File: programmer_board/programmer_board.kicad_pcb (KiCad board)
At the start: 2 copper layers, 99.1 x 86.4 mm, 20 parts, among them J1 8bit_thing_bus_connector, J2 greenpak_i2c, U1 Pico, U2 74AHCT573, U3 74AHCT573, U4 74AHCT573, U5 74LVC245, U6 SLG46826G

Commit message: Pico programmer: remove some redundant traces and fix 3d model
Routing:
- net /D1_OUT: track 89.2 -> 87.5 mm
- net /D6_OUT: track 72.6 -> 71.8 mm
- net /D5_OUT: track 74.5 -> 73.7 mm
- net /D4_OUT: track 79.0 -> 78.2 mm
- net /D3_OUT: track 84.5 -> 83.7 mm
- net /D2_OUT: track 87.4 -> 86.6 mm
- net /D0_OUT: track 91.3 -> 90.5 mm
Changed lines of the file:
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@@
     (pad "20" smd roundrect (at 2.865 -2.925 90) (size 1.48 0.41) (layers "F.Cu" "F.Paste" "F.Mask") (roundrect_rratio 0.05)
       (net 5 "+5V") (pinfunction "VDD") (pintype "power_in"))
+    (model "${KICAD6_3DMODEL_DIR}/Package_SO.3dshapes/TSSOP-20_4.4x6.5mm_P0.65mm.wrl"
+      (offset (xyz 0 0 0))
+      (scale (xyz 1 1 1))
+      (rotate (xyz 0 0 0))
+    )
   )
   (footprint "imported_footprints:RPi_Pico_SMD_TH" (layer "F.Cu")
@@
   (segment (start 107.8445 56.0285) (end 107.569 55.753) (width 0.4) (layer "F.Cu") (net 6))
   (segment (start 85.3225 49.022) (end 85.3225 49.8055) (width 0.4) (layer "F.Cu") (net 6))
-  (segment (start 56.145 61.2035) (end 55.9015 60.96) (width 0.4) (layer "F.Cu") (net 6))
   (segment (start 56.145 63.1775) (end 56.145 64.247205) (width 0.4) (layer "F.Cu") (net 6))
   (segment (start 55.495 67.964797) (end 55.441509 67.911306) (width 0.4) (layer "F.Cu") (net 6))
@@
   (segment (start 78.218837 52.233503) (end 81.086 55.100666) (width 0.2) (layer "F.Cu") (net 43))
   (segment (start 81.086 56.761326) (end 81.855171 57.530497) (width 0.2) (layer "F.Cu") (net 43))
-  (segment (start 93.786 55.930996) (end 93.786 56.761326) (width 0.2) (layer "F.Cu") (net 43))
   (segment (start 81.855171 57.530497) (end 83.058503 57.530497) (width 0.2) (layer "F.Cu") (net 43))
   (segment (start 70.254126 57.546994) (end 73.551501 54.249619) (width 0.2) (layer "F.Cu") (net 43))
@@
   (segment (start 93.136 56.761326) (end 93.472 57.097326) (width 0.2) (layer "F.Cu") (net 44))
   (segment (start 73.951002 54.153558) (end 75.41856 52.686) (width 0.2) (layer "F.Cu") (net 44))
-  (segment (start 93.136 55.930996) (end 93.136 56.761326) (width 0.2) (layer "F.Cu") (net 44))
   (segment (start 75.41856 52.686) (end 78.045 52.686) (width 0.2) (layer "F.Cu") (net 44))
   (segment (start 73.951002 54.415098) (end 73.951002 54.153558) (width 0.2) (layer "F.Cu") (net 44))
@@
   (segment (start 90.600433 53.132493) (end 92.486 55.01806) (width 0.2) (layer "F.Cu") (net 45))
   (segment (start 83.529501 58.329499) (end 86.2965 55.5625) (width 0.2) (layer "F.Cu") (net 45))
-  (segment (start 92.486 55.930996) (end 92.486 56.761326) (width 0.2) (layer "F.Cu") (net 45))
   (segment (start 67.086 56.88394) (end 68.548056 58.345996) (width 0.2) (layer "F.Cu") (net 45))
   (segment (start 92.486 56.761326) (end 92.837 57.112326) (width 0.2) (layer "F.Cu") (net 45))
@@
   (segment (start 74.750004 54.746056) (end 74.750004 54.49429) (width 0.2) (layer "F.Cu") (net 46))
   (segment (start 88.454006 53.531994) (end 90.434954 53.531994) (width 0.2) (layer "F.Cu") (net 46))
-  (segment (start 91.839501 55.934497) (end 91.839501 56.764827) (width 0.2) (layer "F.Cu") (net 46))
   (segment (start 92.202 57.127326) (end 92.202 83.932) (width 0.2) (layer "F.Cu") (net 46))
   (segment (start 75.878278 53.930996) (end 77.511996 53.930996) (width 0.2) (layer "F.Cu") (net 47))
@@
   (segment (start 90.269475 53.931495) (end 91.186 54.84802) (width 0.2) (layer "F.Cu") (net 47))
   (segment (start 77.511996 53.930996) (end 78.486 54.905) (width 0.2) (layer "F.Cu") (net 47))
-  (segment (start 91.186 55.930996) (end 91.186 56.761326) (width 0.2) (layer "F.Cu") (net 47))
   (segment (start 88.624505 53.931495) (end 90.269475 53.931495) (width 0.2) (layer "F.Cu") (net 47))
   (segment (start 87.9865 55.88) (end 87.9865 55.13448) (width 0.2) (layer "F.Cu") (net 48))
@@
   (segment (start 89.76633 54.330996) (end 90.536 55.100666) (width 0.2) (layer "F.Cu") (net 48))
   (segment (start 77.836 56.761326) (end 80.619173 59.544499) (width 0.2) (layer "F.Cu") (net 48))
-  (segment (start 90.536 55.930996) (end 90.536 56.761326) (width 0.2) (layer "F.Cu") (net 48))
   (segment (start 87.9865 55.13448) (end 88.789985 54.330996) (width 0.2) (layer "F.Cu") (net 48))
   (segment (start 77.150702 54.330996) (end 77.836 55.016294) (width 0.2) (layer "F.Cu") (net 48))
@@
   (segment (start 77.836 55.016294) (end 77.836 55.930996) (width 0.2) (layer "F.Cu") (net 48))
   (segment (start 90.932 87.742) (end 106.68 103.49) (width 0.2) (layer "F.Cu") (net 48))
-  (segment (start 90.536 55.100666) (end 90.536 55.930996) (width 0.2) (layer "F.Cu") (net 48))
   (segment (start 90.932 57.157326) (end 90.932 87.742) (width 0.2) (layer "F.Cu") (net 48))
   (segment (start 75.549006 54.825248) (end 76.043258 54.330996) (width 0.2) (layer "F.Cu") (net 48))
@@
   (segment (start 75.549006 55.077014) (end 75.549006 54.825248) (width 0.2) (layer "F.Cu") (net 48))
   (segment (start 80.368674 59.944) (end 84.65731 59.944) (width 0.2) (layer "F.Cu") (net 49))
-  (segment (start 89.886 55.930996) (end 89.886 56.761326) (width 0.2) (layer "F.Cu") (net 49))
   (segment (start 77.186 56.761326) (end 80.368674 59.944) (width 0.2) (layer "F.Cu") (net 49))
   (segment (start 90.297 57.172326) (end 90.297 89.647) (width 0.2) (layer "F.Cu") (net 49))

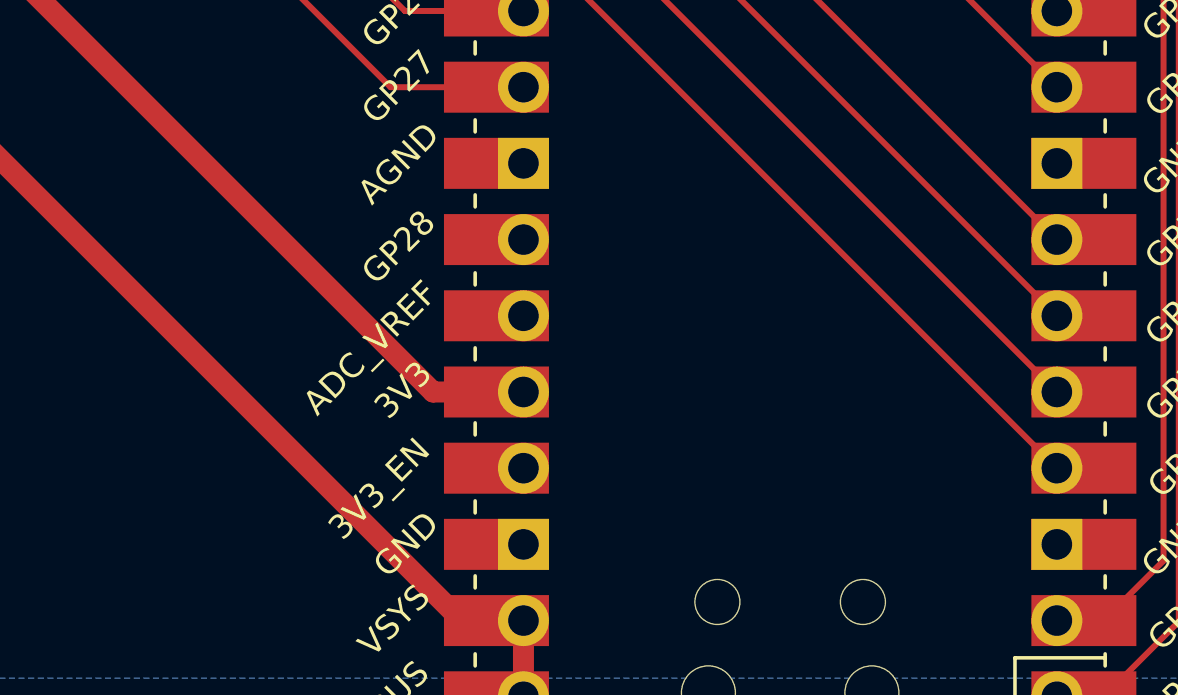
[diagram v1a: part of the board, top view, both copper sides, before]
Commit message: pico board: add more bypass caps, add JLCPCB string
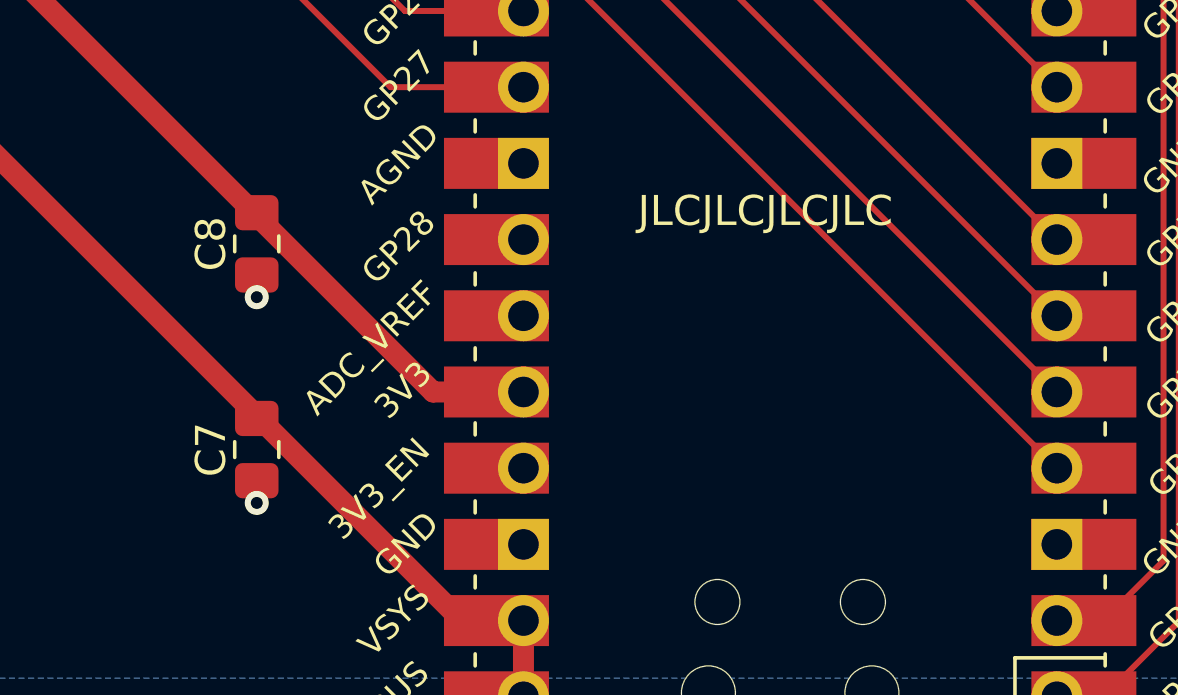
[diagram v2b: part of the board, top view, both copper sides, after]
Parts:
- added C7: 4.7u, Capacitor_SMD:C_0805_2012Metric_Pad1.18x1.45mm_HandSolder, F.Cu at (80.0, 105.4)
- added C8: 4.7u, Capacitor_SMD:C_0805_2012Metric_Pad1.18x1.45mm_HandSolder, F.Cu at (80.0, 98.6)
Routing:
- net GND: track 13.3 -> 14.7 mm, vias 11 -> 13
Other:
- board text added: "JLCJLCJLCJLC"
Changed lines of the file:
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@@
+    )
+  )
+  (footprint "Capacitor_SMD:C_0805_2012Metric_Pad1.18x1.45mm_HandSolder" (layer "F.Cu")
+    (at 80.01 98.552 -90)
+    (descr "Capacitor SMD 0805 (2012 Metric), square (rectangular) end terminal, IPC_7351 nominal with elongated pad for handsoldering. (Body size source: IPC-SM-782 page 76, https://www.pcb-3d.com/wordpress/wp-content/uploads/ipc-sm-782a_amendment_1_and_2.pdf, https://docs.google.com/spreadsheets/d/1BsfQQcO9C6DZCsRaXUlFlo91Tg2WpOkGARC1WS5S8t0/edit?usp=sharing), generated with kicad-footprint-generator")
+    (tags "capacitor handsolder")
+    (property "Sheetfile" "programmer_board.kicad_sch")
+    (property "Sheetname" "")
+    (property "ki_description" "Unpolarized capacitor, small symbol")
+    (property "ki_keywords" "capacitor cap")
+    (attr smd)
+    (fp_text reference "C8" (at 0 1.524 90) (layer "F.SilkS")
+        (effects (font (size 1 1) (thickness 0.15)))
+    )
+    (fp_text value "4.7u" (at 0 1.68 90) (layer "F.Fab")
+        (effects (font (size 1 1) (thickness 0.15)))
+    )
+    (fp_text user "${REFERENCE}" (at 0 0 90) (layer "F.Fab")
+        (effects (font (size 0.5 0.5) (thickness 0.08)))
+    )
+    (fp_line (start -0.261252 -0.735) (end 0.261252 -0.735)
+      (stroke (width 0.12) (type solid)) (layer "F.SilkS"))
+    (fp_line (start -0.261252 0.735) (end 0.261252 0.735)
+      (stroke (width 0.12) (type solid)) (layer "F.SilkS"))
+    (fp_line (start -1.88 -0.98) (end 1.88 -0.98)
+      (stroke (width 0.05) (type solid)) (layer "F.CrtYd"))
+    (fp_line (start -1.88 0.98) (end -1.88 -0.98)
+      (stroke (width 0.05) (type solid)) (layer "F.CrtYd"))
+    (fp_line (start 1.88 -0.98) (end 1.88 0.98)
+      (stroke (width 0.05) (type solid)) (layer "F.CrtYd"))
+    (fp_line (start 1.88 0.98) (end -1.88 0.98)
+      (stroke (width 0.05) (type solid)) (layer "F.CrtYd"))
+    (fp_line (start -1 -0.625) (end 1 -0.625)
+      (stroke (width 0.1) (type solid)) (layer "F.Fab"))
+    (fp_line (start -1 0.625) (end -1 -0.625)
+      (stroke (width 0.1) (type solid)) (layer "F.Fab"))
+    (fp_line (start 1 -0.625) (end 1 0.625)
+      (stroke (width 0.1) (type solid)) (layer "F.Fab"))
+    (fp_line (start 1 0.625) (end -1 0.625)
+      (stroke (width 0.1) (type solid)) (layer "F.Fab"))
+    (pad "1" smd roundrect (at -1.0375 0 270) (size 1.175 1.45) (layers "F.Cu" "F.Paste" "F.Mask") (roundrect_rratio 0.212766)
+      (net 15 "+3.3V") (pintype "passive"))
+    (pad "2" smd roundrect (at 1.0375 0 270) (size 1.175 1.45) (layers "F.Cu" "F.Paste" "F.Mask") (roundrect_rratio 0.212766)
+      (net 6 "GND") (pintype "passive"))
+    (model "${KICAD6_3DMODEL_DIR}/Capacitor_SMD.3dshapes/C_0805_2012Metric.wrl"
+      (offset (xyz 0 0 0))
+      (scale (xyz 1 1 1))
+      (rotate (xyz 0 0 0))
     )
   )
@@
       (net 71 "unconnected-(U1-SWDIO-Pad43)") (pinfunction "SWDIO") (pintype "bidirectional+no_connect"))
     (model "${IMPORTED}/Pico.wrl"
+      (offset (xyz 0 0 0))
+      (scale (xyz 1 1 1))
+      (rotate (xyz 0 0 0))
+    )
+  )
+  (footprint "Capacitor_SMD:C_0805_2012Metric_Pad1.18x1.45mm_HandSolder" (layer "F.Cu")
+    (at 80.01 105.41 -90)
+    (descr "Capacitor SMD 0805 (2012 Metric), square (rectangular) end terminal, IPC_7351 nominal with elongated pad for handsoldering. (Body size source: IPC-SM-782 page 76, https://www.pcb-3d.com/wordpress/wp-content/uploads/ipc-sm-782a_amendment_1_and_2.pdf, https://docs.google.com/spreadsheets/d/1BsfQQcO9C6DZCsRaXUlFlo91Tg2WpOkGARC1WS5S8t0/edit?usp=sharing), generated with kicad-footprint-generator")
+    (tags "capacitor handsolder")
+    (property "Sheetfile" "programmer_board.kicad_sch")
+    (property "Sheetname" "")
+    (property "ki_description" "Unpolarized capacitor, small symbol")
+    (property "ki_keywords" "capacitor cap")
+    (attr smd)
+    (fp_text reference "C7" (at 0 1.524 90) (layer "F.SilkS")
+        (effects (font (size 1 1) (thickness 0.15)))
+    )
+    (fp_text value "4.7u" (at 0 1.68 90) (layer "F.Fab")
+        (effects (font (size 1 1) (thickness 0.15)))
+    )
+    (fp_text user "${REFERENCE}" (at 0 0 90) (layer "F.Fab")
+        (effects (font (size 0.5 0.5) (thickness 0.08)))
+    )
+    (fp_line (start -0.261252 -0.735) (end 0.261252 -0.735)
+      (stroke (width 0.12) (type solid)) (layer "F.SilkS"))
+    (fp_line (start -0.261252 0.735) (end 0.261252 0.735)
+      (stroke (width 0.12) (type solid)) (layer "F.SilkS"))
+    (fp_line (start -1.88 -0.98) (end 1.88 -0.98)
+      (stroke (width 0.05) (type solid)) (layer "F.CrtYd"))
+    (fp_line (start -1.88 0.98) (end -1.88 -0.98)
+      (stroke (width 0.05) (type solid)) (layer "F.CrtYd"))
+    (fp_line (start 1.88 -0.98) (end 1.88 0.98)
+      (stroke (width 0.05) (type solid)) (layer "F.CrtYd"))
+    (fp_line (start 1.88 0.98) (end -1.88 0.98)
+      (stroke (width 0.05) (type solid)) (layer "F.CrtYd"))
+    (fp_line (start -1 -0.625) (end 1 -0.625)
+      (stroke (width 0.1) (type solid)) (layer "F.Fab"))
+    (fp_line (start -1 0.625) (end -1 -0.625)
+      (stroke (width 0.1) (type solid)) (layer "F.Fab"))
+    (fp_line (start 1 -0.625) (end 1 0.625)
+      (stroke (width 0.1) (type solid)) (layer "F.Fab"))
+    (fp_line (start 1 0.625) (end -1 0.625)
+      (stroke (width 0.1) (type solid)) (layer "F.Fab"))
+    (pad "1" smd roundrect (at -1.0375 0 270) (size 1.175 1.45) (layers "F.Cu" "F.Paste" "F.Mask") (roundrect_rratio 0.212766)
+      (net 5 "+5V") (pintype "passive"))
+    (pad "2" smd roundrect (at 1.0375 0 270) (size 1.175 1.45) (layers "F.Cu" "F.Paste" "F.Mask") (roundrect_rratio 0.212766)
+      (net 6 "GND") (pintype "passive"))
+    (model "${KICAD6_3DMODEL_DIR}/Capacitor_SMD.3dshapes/C_0805_2012Metric.wrl"
       (offset (xyz 0 0 0))
       (scale (xyz 1 1 1))
@@
     (effects (font (size 2.5 2.5) (thickness 0.4)) (justify left))
   )
+  (gr_text "JLCJLCJLCJLC" (at 92.71 98.044) (layer "F.SilkS")
+    (effects (font (size 1 1) (thickness 0.15)) (justify left bottom))
+  )
   (gr_text "SCL" (at 112.395 45.72) (layer "F.SilkS")
     (effects (font (size 1 1) (thickness 0.15)))
@@
   (segment (start 107.513 55.697) (end 107.569 55.753) (width 0.4) (layer "F.Cu") (net 6))
   (segment (start 107.8445 57.785) (end 107.8445 56.0285) (width 0.4) (layer "F.Cu") (net 6))
+  (segment (start 80.01 99.5895) (end 80.01 100.33) (width 0.4) (layer "F.Cu") (net 6))
+  (segment (start 80.01 106.4475) (end 80.01 107.188) (width 0.4) (layer "F.Cu") (net 6))
   (segment (start 59.182 49.022) (end 59.055 49.149) (width 0.4) (layer "F.Cu") (net 6))
   (segment (start 61.6535 68.9025) (end 61.722 68.834) (width 0.4) (layer "F.Cu") (net 6))
@@
   (segment (start 72.6225 49.276) (end 72.6225 50.0165) (width 0.4) (layer "F.Cu") (net 6))
   (segment (start 56.145 63.1775) (end 56.145 61.2035) (width 0.4) (layer "F.Cu") (net 6))
+  (via (at 80.01 107.188) (size 0.8) (drill 0.4) (layers "F.Cu" "B.Cu") (net 6))
   (via (at 85.217 49.911) (size 0.8) (drill 0.4) (layers "F.Cu" "B.Cu") (net 6))
   (via (at 55.441509 67.911306) (size 0.8) (drill 0.4) (layers "F.Cu" "B.Cu") (net 6))
@@
   (via (at 82.677 55.88) (size 0.8) (drill 0.4) (layers "F.Cu" "B.Cu") (net 6))
   (via (at 69.724831 54.735798) (size 0.8) (drill 0.4) (layers "F.Cu" "B.Cu") (net 6))
+  (via (at 80.01 100.33) (size 0.8) (drill 0.4) (layers "F.Cu" "B.Cu") (net 6))
   (via (at 72.644 50.038) (size 0.8) (drill 0.4) (layers "F.Cu" "B.Cu") (net 6))
   (via (at 56.145 64.247205) (size 0.8) (drill 0.4) (layers "F.Cu" "B.Cu") (net 6))

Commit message: Pico board: add i2c pullups
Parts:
- added R1: 10k, Resistor_SMD:R_0805_2012Metric_Pad1.20x1.40mm_HandSolder, F.Cu at (112.5, 48.3)
- added R2: 10k, Resistor_SMD:R_0805_2012Metric_Pad1.20x1.40mm_HandSolder, F.Cu at (112.5, 45.7)
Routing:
- net /~{STBY}: track 55.3 -> 59.6 mm
- net +5V: track 215.7 -> 219.5 mm
- net +3.3V: track 174.4 -> 177.3 mm

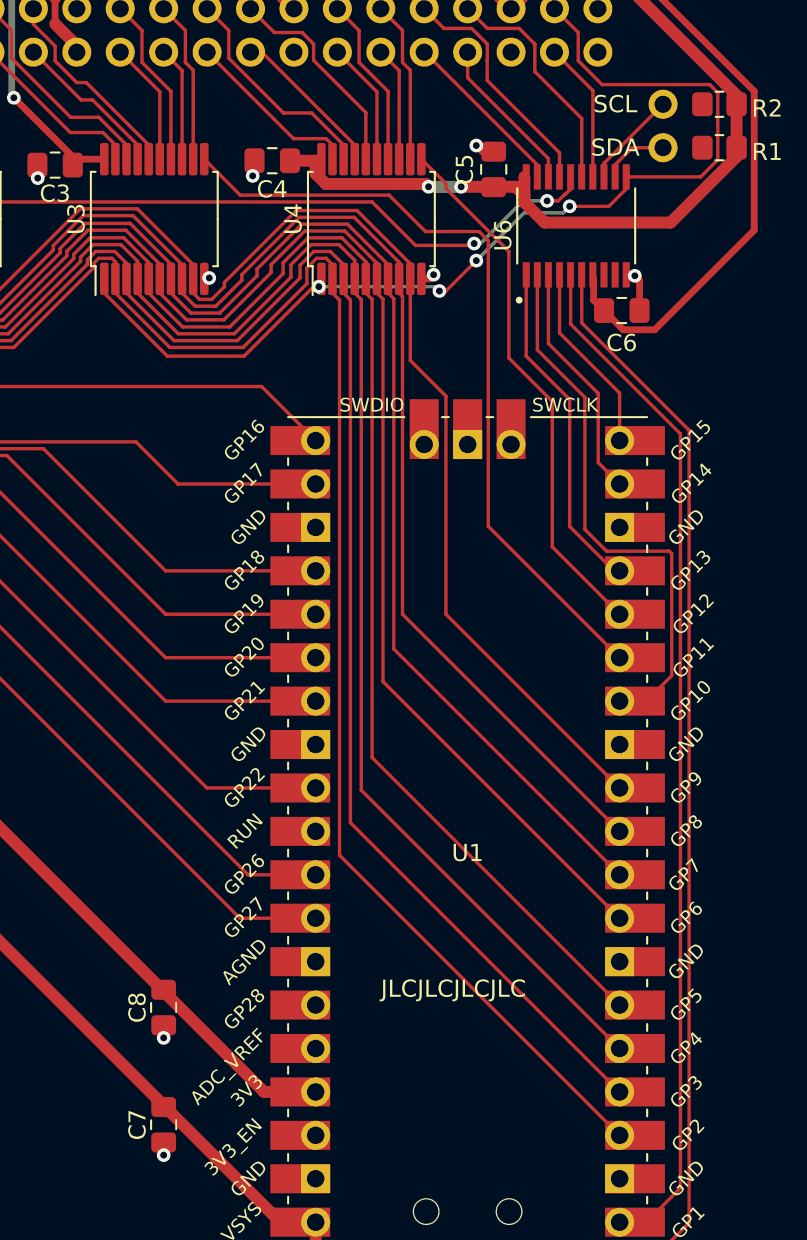
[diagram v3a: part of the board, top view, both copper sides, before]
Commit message: pico board: low address latch needs independent OE to not conflict with latch on HD6301 board
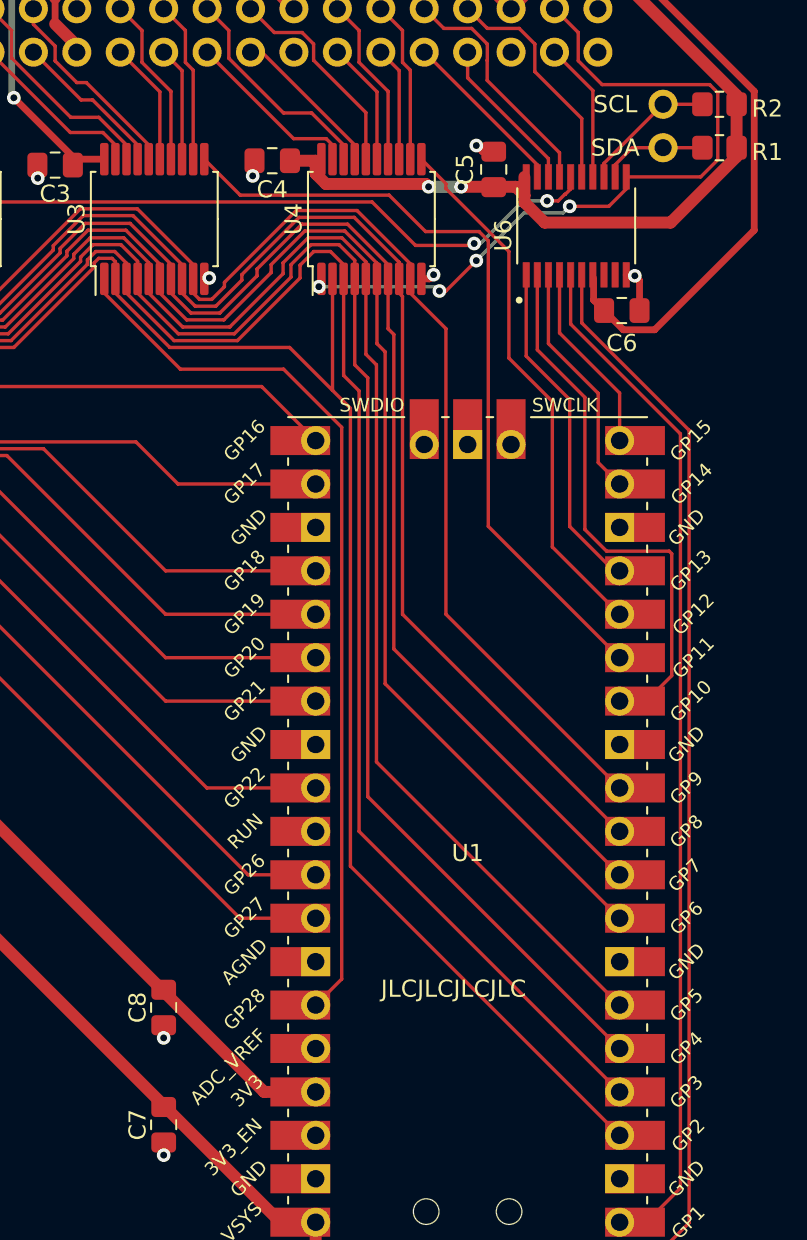
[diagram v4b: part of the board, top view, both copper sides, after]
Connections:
- U1 pad 34: unconnected-(U1-GPIO28_ADC2-Pad34) -> /~{A_L_OE}
- U3 pad 1: /~{STBY} -> /~{A_L_OE}
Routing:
- net /~{A_L_OE}: track 0.00 -> 52.4 mm
- net /~{STBY}: track 59.6 -> 43.5 mm
- net Net-(J2-Pin_2): track 3.93 -> 6.23 mm
- net Net-(J2-Pin_1): track 5.68 -> 7.98 mm
- net /D0_OUT: track 90.5 -> 88.7 mm
